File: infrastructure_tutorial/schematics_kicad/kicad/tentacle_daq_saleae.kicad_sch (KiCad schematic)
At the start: 3 parts, among them T901 tentacle, T902 tentacle, T903 tentacle

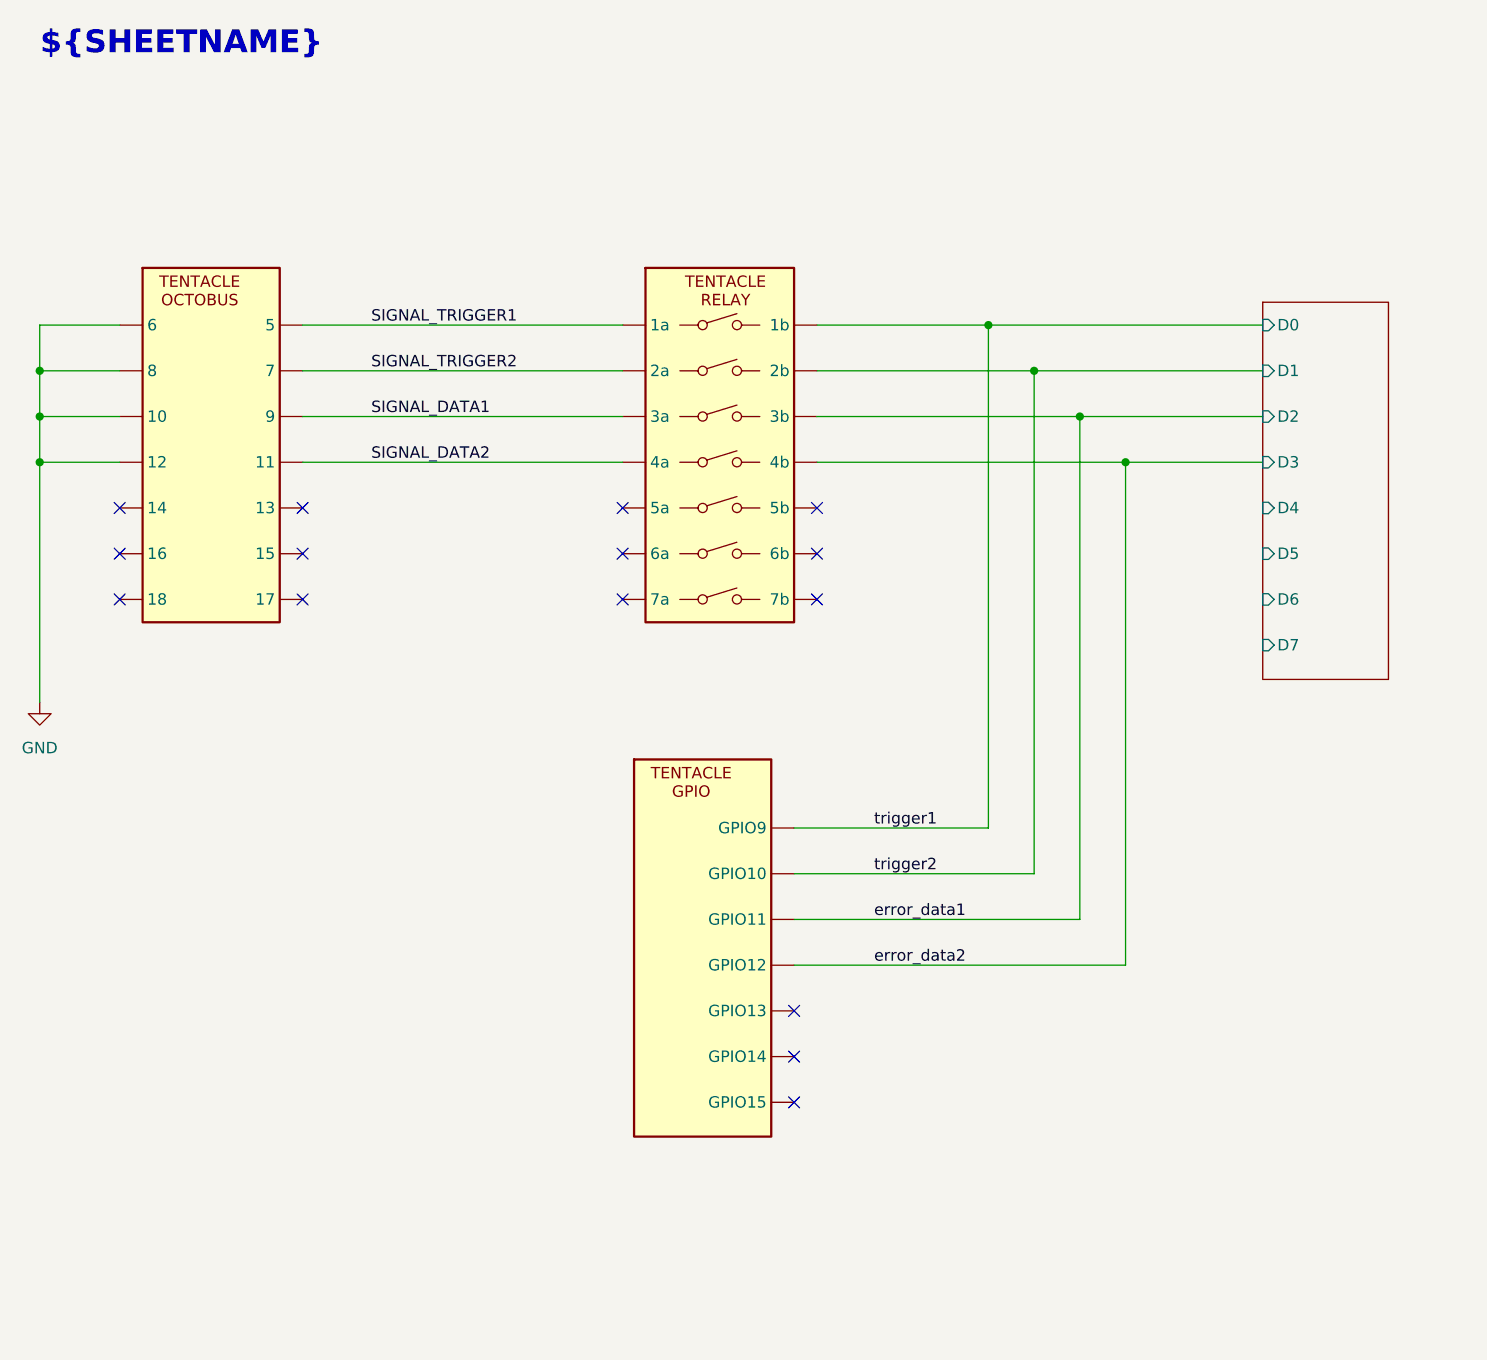
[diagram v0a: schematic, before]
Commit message: pytest for infrastructure_tutorial
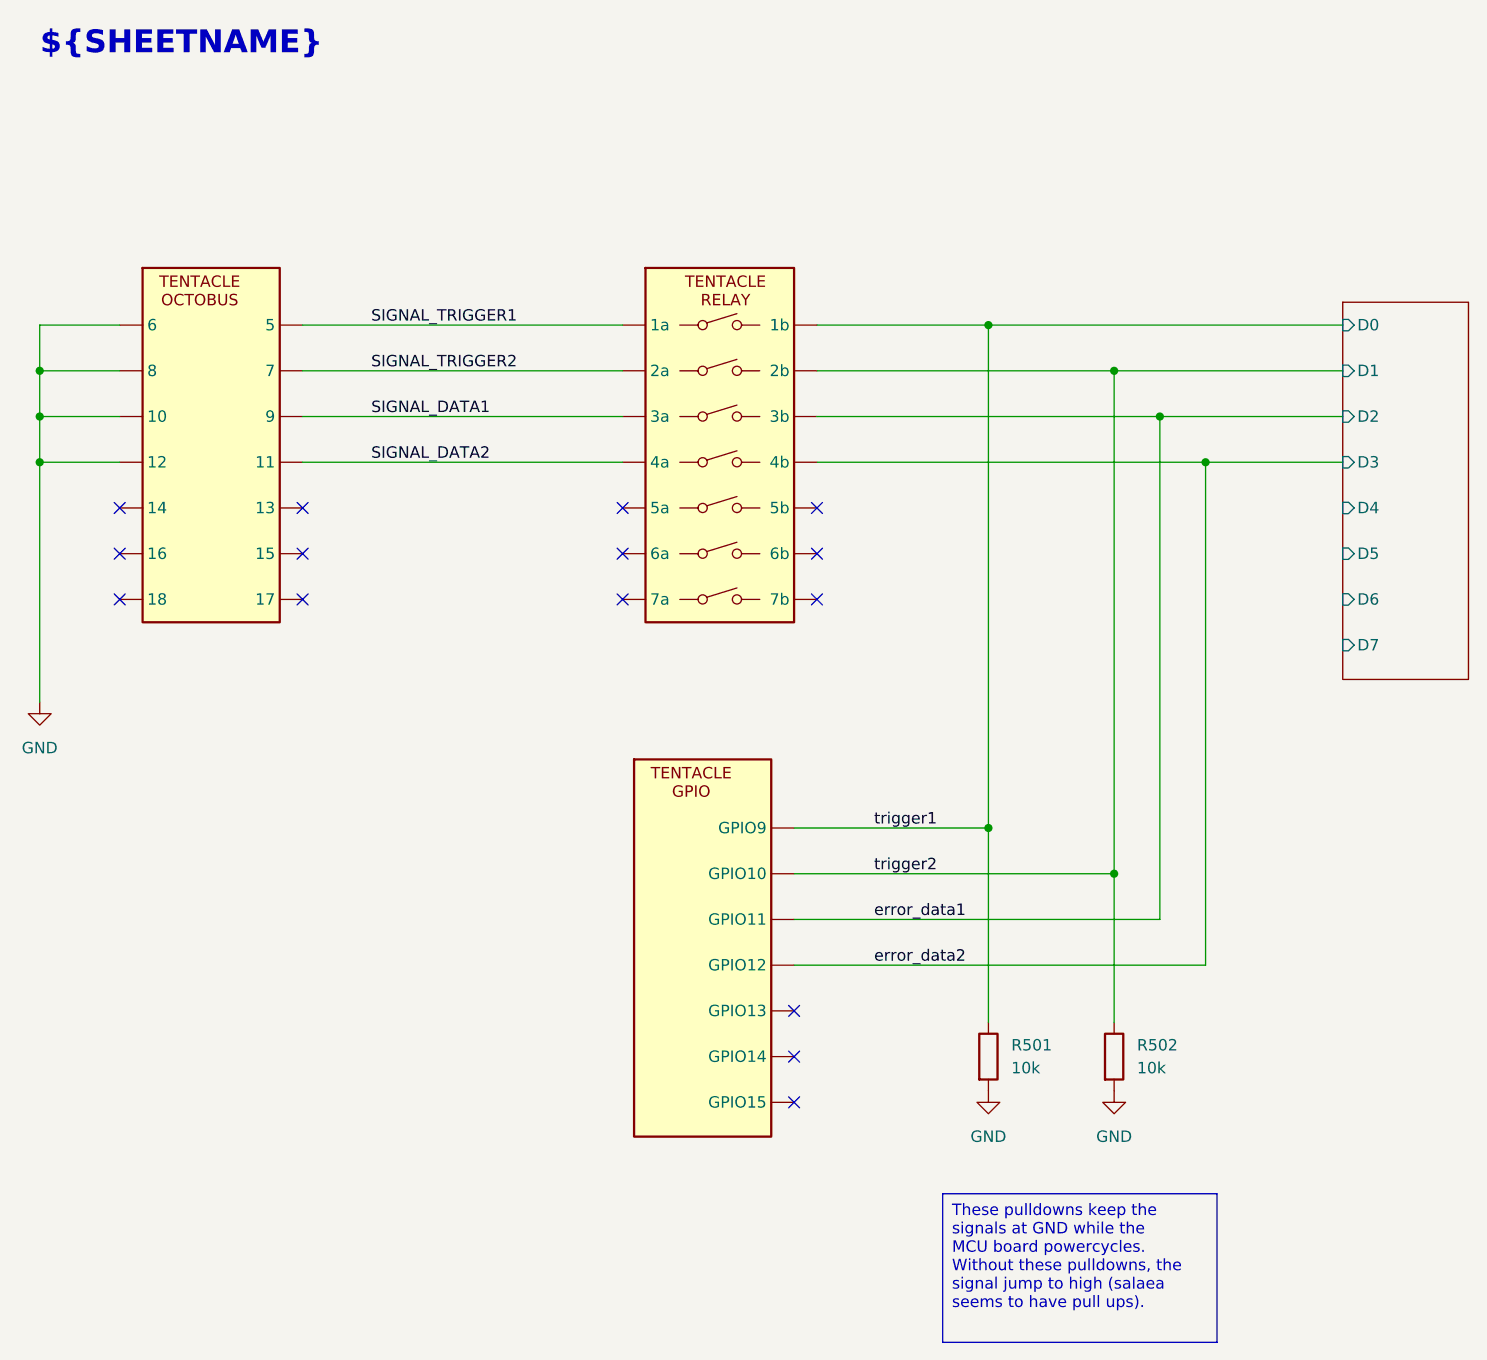
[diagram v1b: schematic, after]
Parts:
- added R501, R502: 10k, symbol Device:R
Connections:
- net GND: now also R501.2, R502.2
- net trigger1: now also R501.1
- net trigger2: now also R502.1
